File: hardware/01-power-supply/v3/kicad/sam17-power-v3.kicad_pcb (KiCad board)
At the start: 2 copper layers, 200 x 150 mm, 114 parts, among them J1 Barrier block 3 pos, J2 Molex KK-254 4 pos, J3 Barrier block 3 pos, J4 Barrier block 2 pos, J5 Faston macho 6.3mm PCB, J6 Molex KK-254 2 pos, J7 Barrier block 2 pos, J8 JST-PH 4 pos, U1 LM2941CT/NOPB, U10 ADS1115IDGSR — ADC 16 bits 4 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, U11 TMP1075DGKR — sensor de tempe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, U12 ISO1541D — aislador I2C bidir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, U2 LM2991T/NOPB, U3 LM7805, U4 LT3045EDD#TRPBF, U5 LT3045EDD#TRPBF, U6 LT3094EDD#PBF, U7 LT3094EDD#PBF, U8 INA226AIDGSR — monitor I/V I2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, U9 INA226AIDGSR — monitor I/V I2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

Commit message: Cero conexiones sin rutear, y el filler de KiCad se cae con la placa terminada
126 elementos sin conectar -> 0. DRC real: 48 infracciones -> 10, y ninguna
de las diez es de cobre.

    clearance          0     (eran 34)
    cortos             0
    hole_to_hole       0     (era 1)
    sin conectar       0     (eran 126)
    silk_overlap       5     cosmetica, pendiente
    track_dangling     3     tres rabitos de 0.5 mm sin enganchar
    isolated_copper    1     la zona GNDREF, ver abajo

## Tres cosas que estaban mal y no eran del ruteo

**El EP de U6/U7 no llegaba a ningun sitio.** Salia 2.5 mm al sur y ahi se
quedaba: la entrada de los dos LT3094 estaba conectada solo por sus pines
1-3. Las puertas propias no lo veian porque miden SEPARACION, no
continuidad; el DRC real si. Ahora baja a y=55.5 -- por debajo de la fila de
pines, que acaba en 54.25 -- y entra al canal vertical de su mitad de la isla.

**F1 tiene dos clips por lado.** Su huella trae dos pads numerados "1" y dos
numerados "2", y la cadena de red entraba por uno de cada par: el
portafusible tiene dos posiciones y solo una estaba cableada.

**+12V eran dos islas.** El canal de x=19.5 con R15.2 y D10.2 por un lado, y
el de x=41.5 con R16.2, el shunt y TP3 por otro, sin nada que los una. El
laberinto no lo veia porque cada pad tocaba ALGUN cobre de su red: ahora se
calculan los componentes conexos y solo el mayor cuenta como "ya conectado".

## Dos trampas de la herramienta, las dos medidas

**`ZONE_FILLER.Fill()` hace SEGFAULT** desde el Python de KiCad 10.0 con esta
placa ya ruteada: exit 139, sin traceback, con 1042 segmentos (con 995
todavia pasaba). No es la zona -- quitando el recorte de H4 tambien peta, y
sin la zona la placa sale entera en verde. El relleno se delega a
`kicad-cli pcb drc --refill-zones --save-board`, que es el mismo codigo
fuera del proceso y no se cae.

**Y la netclass se escapo por segunda vez.** La ronda anterior la escribia en
el .kicad_pro; `kicad-cli --save-board` la devolv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
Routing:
- net /GNDREF: track 0.00 -> 116.0 mm, vias 0 -> 8
- net +12V: track 226.6 -> 260.8 mm, vias 4 -> 6
- net /-12V9: track 383.3 -> 393.3 mm
- net Net-(U7-ILIM): track 5.71 -> 12.2 mm, vias 0 -> 2
- net /L_F: track 123.4 -> 128.5 mm
- net /L: track 32.0 -> 37.1 mm
- net Net-(U6-ILIM): vias 0 -> 2

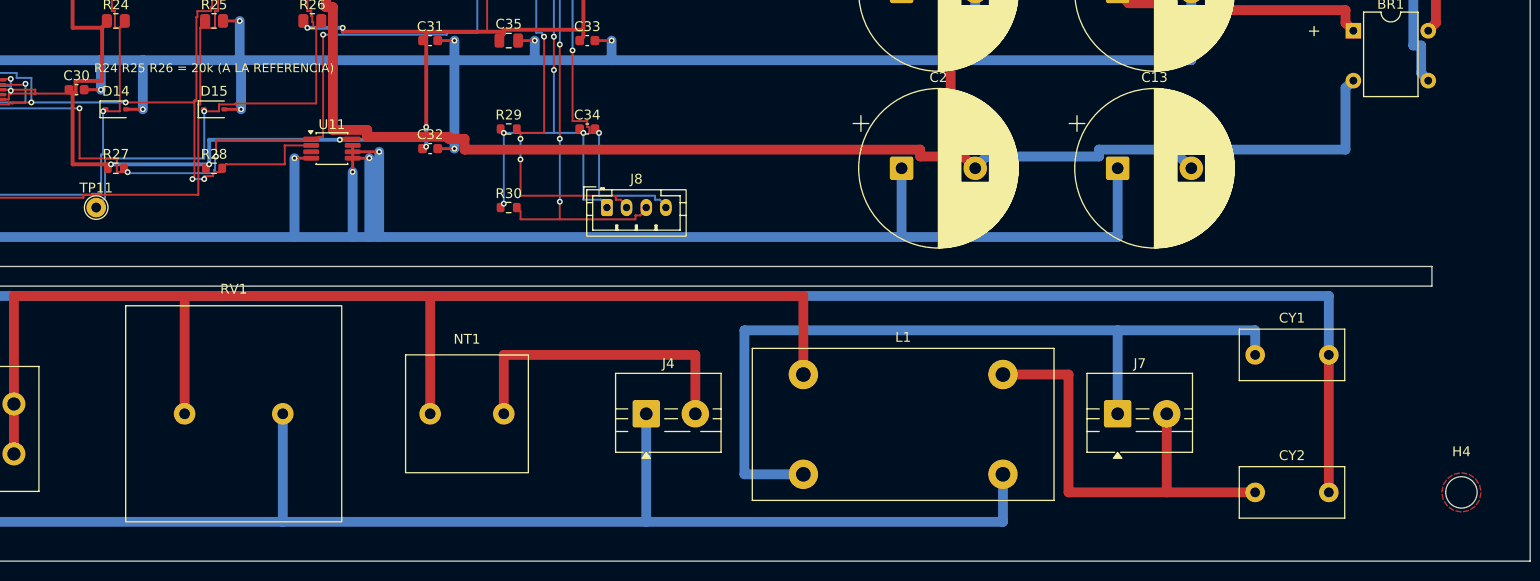
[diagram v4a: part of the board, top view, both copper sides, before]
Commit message: La isla de referencia se rellenaba a 140 mm de donde tenia que estar
DRC real: 0 infracciones y 0 elementos sin conectar. Eran 48 y 126 al
empezar la fase.

## El recorte de H4 apuntaba fuera de su propio poligono

La zona de GNDREF cubre ISLA_REF, que son 3256 mm2 sobre (10,12)-(54,86). Lo
que habia en la placa era **un trozo de 12.24 mm2 centrado en (193, 143)**,
o sea alrededor del taladro H4 y en la esquina opuesta.

El recorte circular de H4 se escribio cuando la placa media 150x200 y el
taladro caia dentro de la isla. Al girarla a 200x150 (Task 6) H4 se fue a
(193, 143) y el recorte se quedo: un "agujero" fuera del contorno que lo
contiene, que es geometria invalida. El comentario del codigo seguia diciendo
"H4 cae DENTRO de ISLA_REF" -- ya no.

De ahi salian, todos a la vez, el `isolated_copper` del DRC y los seis pads
de GNDREF sin conectar. Ahora el recorte se calcula: se recorta el taladro
que de verdad caiga dentro, y si no cae ninguno no se recorta ninguno. Son
cero. La zona pasa a rellenar 1664.8 mm2 en dos trozos, el mayor de 1514 mm2
centrado en (28.5, 43.4).

**El segfault del ZONE_FILLER no era esto.** Se probo a proposito con el
poligono ya arreglado y se sigue cayendo: son dos fallos independientes y el
relleno se queda delegado en `kicad-cli --refill-zones --save-board`.

## Lo demas de esta ronda

* **Tres rabitos de 0.5 mm colgando.** El remate al centro del pad se
  insertaba en el primer tramo del camino, y ese tramo puede estar en B.Cu:
  una pista de B.Cu naciendo en un pad SMD que solo existe en F.Cu. Ahora se
  remata solo en una capa donde el pad tenga cobre. (Y el primer intento
  comparaba un entero de capa contra un nombre: siempre falso, dejo de
  rematar en los 19 sitios donde si hacia falta. Corregido.)
* **Seis choques de serigrafia.** Las referencias de C2 y C13 caian entre la
  seda del bulk de arriba y la del suyo -- 0.45 mm sobre un minimo de 0.5 --
  y debajo tampoco cabian: ahi empieza la ranura de la barrera de red. Van al
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
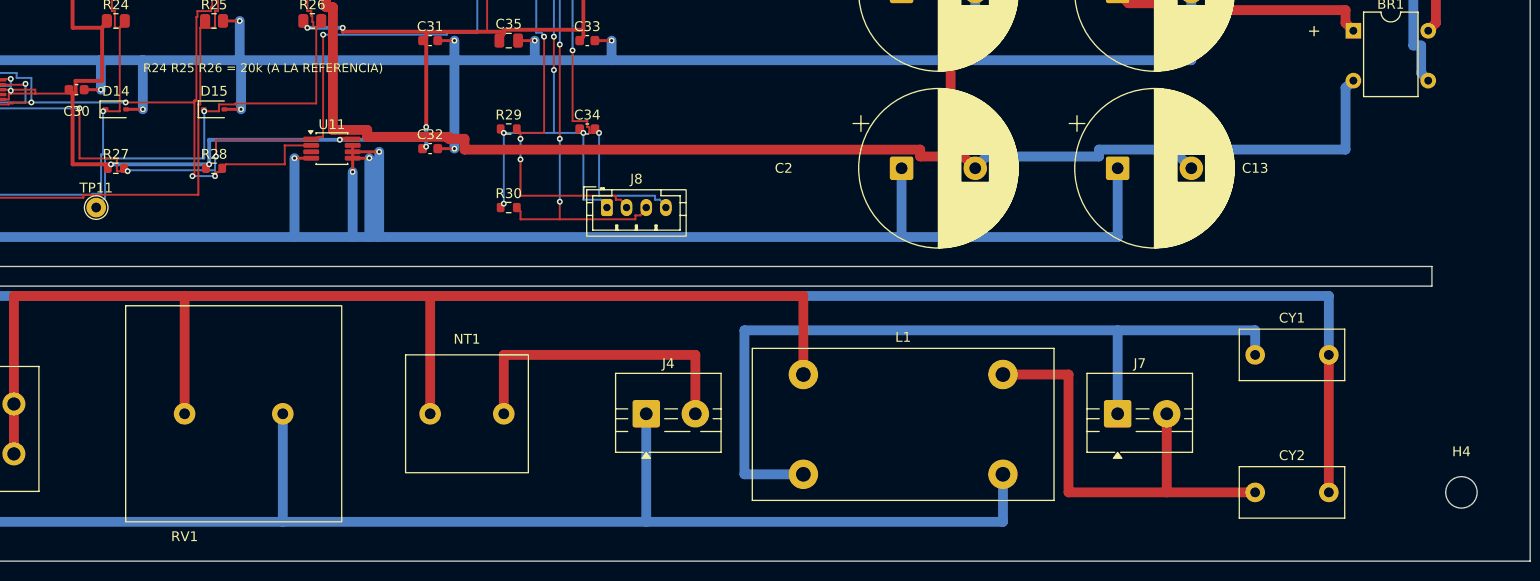
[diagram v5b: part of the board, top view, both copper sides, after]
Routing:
- net +3V3: track 48.6 -> 47.5 mm
- net /SCL_A: track 141.7 -> 141.1 mm
- net /SDA_A: track 132.3 -> 131.7 mm
- net +5V: track 345.4 -> 344.9 mm

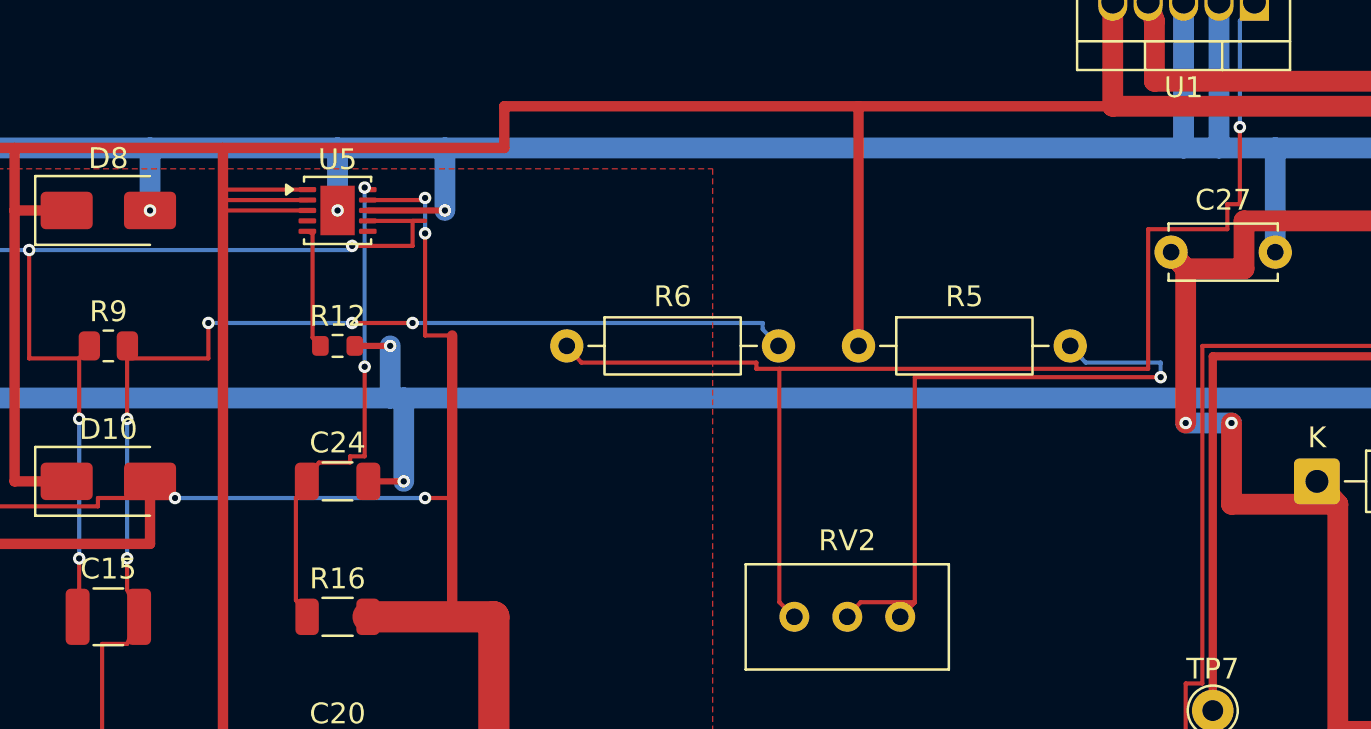
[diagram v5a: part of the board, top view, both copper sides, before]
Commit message: R6 estaba dibujado espejado de R8, y su pad de referencia nunca estuvo conectado
DRC real: 0 infracciones, 0 elementos sin conectar. Todas las puertas propias
en verde, incluida `revisar_isla_referencia()`, que era la ultima en rojo.

## El hallazgo

R6 y R8 son el mismo divisor de ajuste a cada lado de la placa, con la misma
huella y la misma colocacion. En el esquematico estan dibujados espejados --
R6 lleva GNDREF abajo y R8 arriba -- asi que el pin que toca la referencia es
el 2 en uno y el 1 en el otro.

En la PLACA eso manda el pad de GNDREF de R6 a x=57.16. ISLA_REF acaba en
x=54: ni la zona lo alcanzaba ni una pista puede llegar sin sacar la
referencia de su isla. **R6.2 no ha estado conectado en ninguna version de
esta fuente**, y R6 es el fondo del divisor de ajuste de U1, el pre-regulador
de +12 V.

No se vio antes porque la puerta que lo vigila solo mira PISTAS de GNDREF, y
hasta esta tanda no habia ninguna: era verde por vacia. Es el Principio VIII
de la constitucion aplicandose solo -- una comprobacion que nunca se ha visto
fallar no es una comprobacion.

## El arreglo

Girar el simbolo de R6 180 grados. El cableado del esquematico no se mueve ni
un milimetro y la huella tampoco -- un resistor es simetrico -- pero el pad
que lleva GNDREF pasa a ser el 1, que esta en x=47 y dentro de la isla, igual
que el de R8.

El golden lo caza y por eso existe:

    -GNDREF:        C15-2 C16-2 JP1-1 R10-2 R6-2 R8-1 R9-2
    +GNDREF:        C15-2 C16-2 JP1-1 R10-2 R6-1 R8-1 R9-2
    -Net-(U1-ADJ):  R6-1 RV2-3 U1-1
    +Net-(U1-ADJ):  R6-2 RV2-3 U1-1

Dos lineas, y ninguna otra red se movio.

## Estado de las puertas

    check_netlist.py   OK -- shunts en serie, tres divisores en su sentido,
                       los cinco chips en el I2C, barrera de masas sin un
                       nodo comun
    check_bom.py       OK -- 110 en la hoja, 114 designadores
    netdiff            golden actualizado, solo estas dos redes
    DRC (kicad-cli)    0 infracciones, 0 sin c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
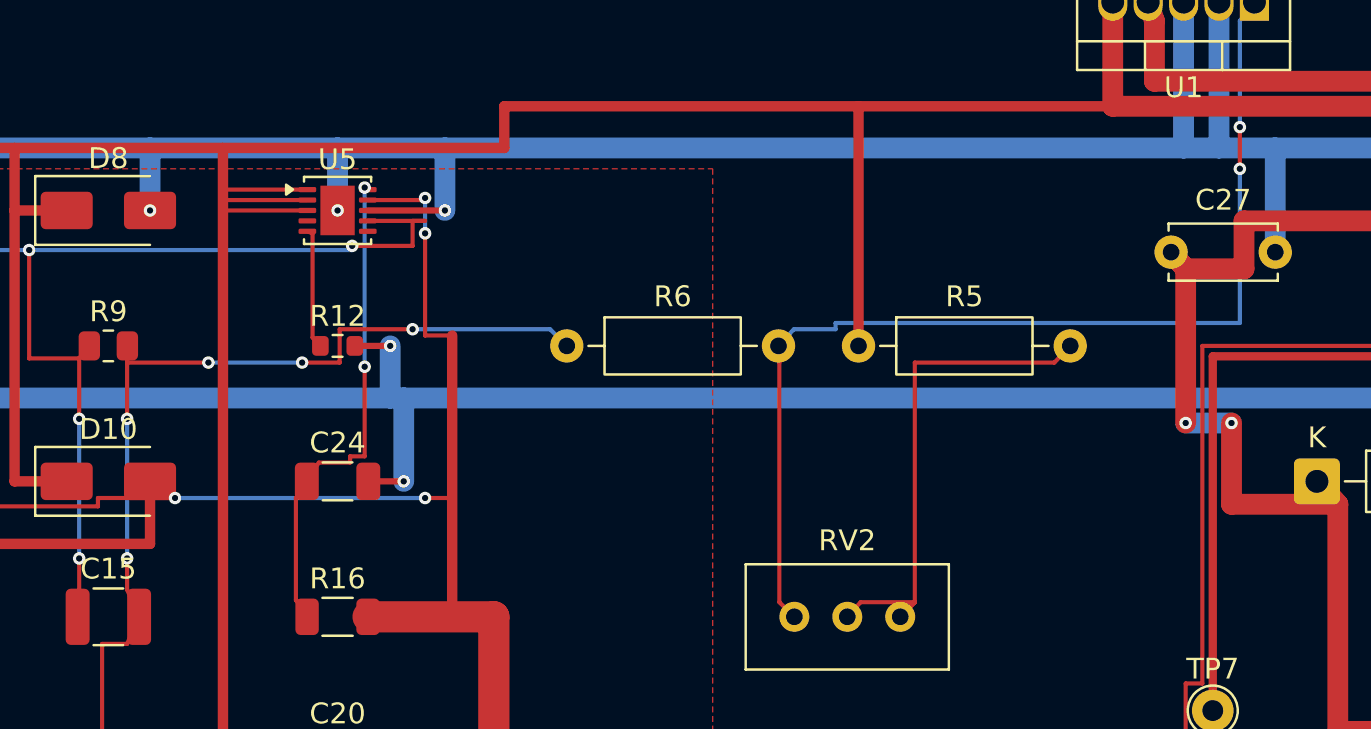
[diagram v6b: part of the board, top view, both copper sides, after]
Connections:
- R6 pad 1: Net-(U1-ADJ) -> /GNDREF
- R6 pad 2: /GNDREF -> Net-(U1-ADJ)
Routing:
- net Net-(U1-ADJ): track 63.0 -> 51.7 mm, vias 1 -> 2
- net /GNDREF: track 116.0 -> 104.8 mm
- net Net-(R5-Pad2): track 33.5 -> 24.8 mm, vias 1 -> 0

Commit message: Dos fusibles en serie en el mismo primario, y ninguno sabia cual miraba
Cierra la parte del #130 que tocaba la PCB. `F1` sale de la placa: el fusible
de red se queda en el IEC C14 de la pared del recinto.

## El desfase

La spec del case §7 lo dice desde el principio, dos veces -- "entrada IEC C14
con portafusible + interruptor" -- y `F1` estaba ademas en la placa. Nadie
habia cruzado los dos documentos. Dos fusibles en serie en el mismo primario
es peor que uno solo: el mismo fallo los ve a los dos y no hay forma de saber
cual miro.

Se queda el del IEC porque es el ACCESIBLE. Cambiar `F1` obligaba a abrir un
recinto de acero cerrado.

**El requisito no se va con la pieza**, y eso queda escrito en design-notes
§14.2 y en el README de fab: el fusible del chasis tiene que ser 1.6 A lento
-- por el inrush del toroide de 120 VA mas los 0.2 A de la SMPS -- y su
portafusible **cerrado**, que es lo que pide haber elegido aislamiento
reforzado. Si el IEC que se compre no cumple las dos, no vale: la placa ya no
tiene red detras.

## Lo que cambia

    redes            60 -> 59   (`L` y `L_F` eran el mismo nodo sin F1 en medio)
    nodos           303 -> 301
    pads de red      23 -> 19   (los cuatro clips del portafusible)
    DRC               0 infracciones, 0 sin conectar
    las 7 puertas     en verde

`L_F` significaba "L despues del fusible" y aqui ya no hay fusible: lo que
entra por J3 es `L`, sin mas. El invariante de `check_netlist.py` se reescribe
contra ese nombre y sigue vigilando LO MISMO -- de que nodo cuelga el choke de
la SMPS: antes de NT1, porque el limitador esta dimensionado para TR1 y la
SMPS no debe compartirlo (spec v2 §7).

## Y una regla que medía la serigrafía

Al re-rutear salio que `revisar_diagonal()` habia bajado de 40 a 32 mm sobre
un umbral de 30. La causa no era electrica: `bbox_de()` usaba
`GetBoundingBox()` a secas, que **cuenta el texto**, y en la ronda anterior yo
habia movido la referencia "C2" por un choque de serigrafia. Ocho milimet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
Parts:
- removed F1: Fusible 1.6A lento + portafusible CERRADO 5x20, Fuseholder_Cylinder-5x20mm_Schurter_FPG4_Vertical_Closed
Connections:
- L1 pad 1: /L_F -> /L
- NT1 pad 1: /L_F -> /L
- RV1 pad 1: /L_F -> /L
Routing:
- net /L_F: track 128.5 -> 0.00 mm
- net /L: track 37.1 -> 150.0 mm

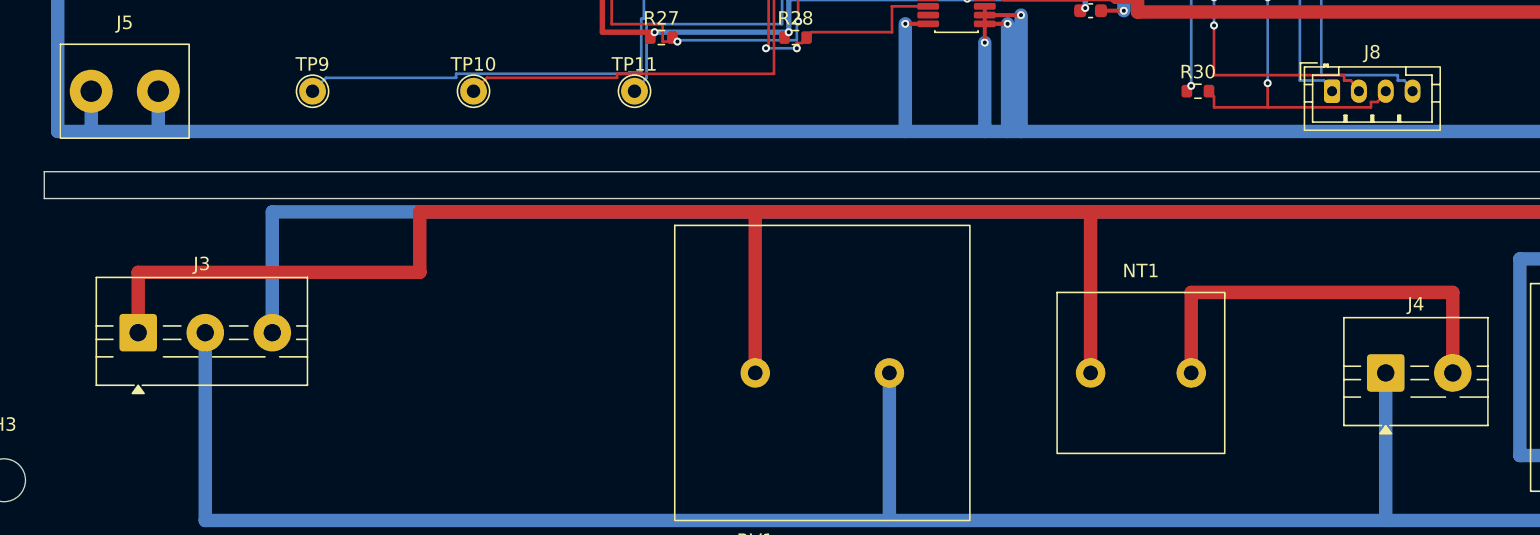
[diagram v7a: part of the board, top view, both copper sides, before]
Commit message: La placa regenerada con las huellas buenas, y un literal que dependia de una
NT1 movio un pad 2,4 mm al pasar a su huella real (paso 5,1 y no 7,5), asi que
esto es esquematico, netlist, placa, relleno de zona y las siete salidas de
fabricacion otra vez.

Y saco a la luz una cota escrita dos veces: el 95.5 de rutear_red() era la x
del pad 2 CON LA HUELLA VIEJA. Al mover el paso, la subida de NT1.2 arrancaba
en el aire. Ahora se pide con pad_xy(), como sus dos vecinos de arriba -- un
literal que depende de una huella es la misma cota en dos sitios, y solo uno
de los dos se entera cuando cambia.

  DRC (kicad-cli, --severity-all)   0 infracciones  0 sin conectar  0 paridad
  ruteo                             1024 segmentos (antes 1033), 176 vias
  netdiff                           VERDE -- la conectividad no se movio
  barrera de red                    10,63 mm entre pads
                                     7,99 mm sobre el cobre del gerber
  zona GNDREF en el gerber          2159 mm2 de cobre relleno
  cpl                               42 designadores, ninguno con rotacion != 0

El .drl cambia en tres sitios y por eso habia que reexportarlo: el MOV pasa de
1,1 a 1,3, el faston de 1,6 a 1,3 y el NTC de 1,1 a 0,8. Un taladro solo
existe en el drill: el .kicad_pcb no se manda a fabricar.

Co-Authored-By: Claude Sonnet 5 <noreply@anthropic.com>
Claude-Session: https://claude.ai/code/session_01B8kQ36zt3gJuqVVwrKaJzk
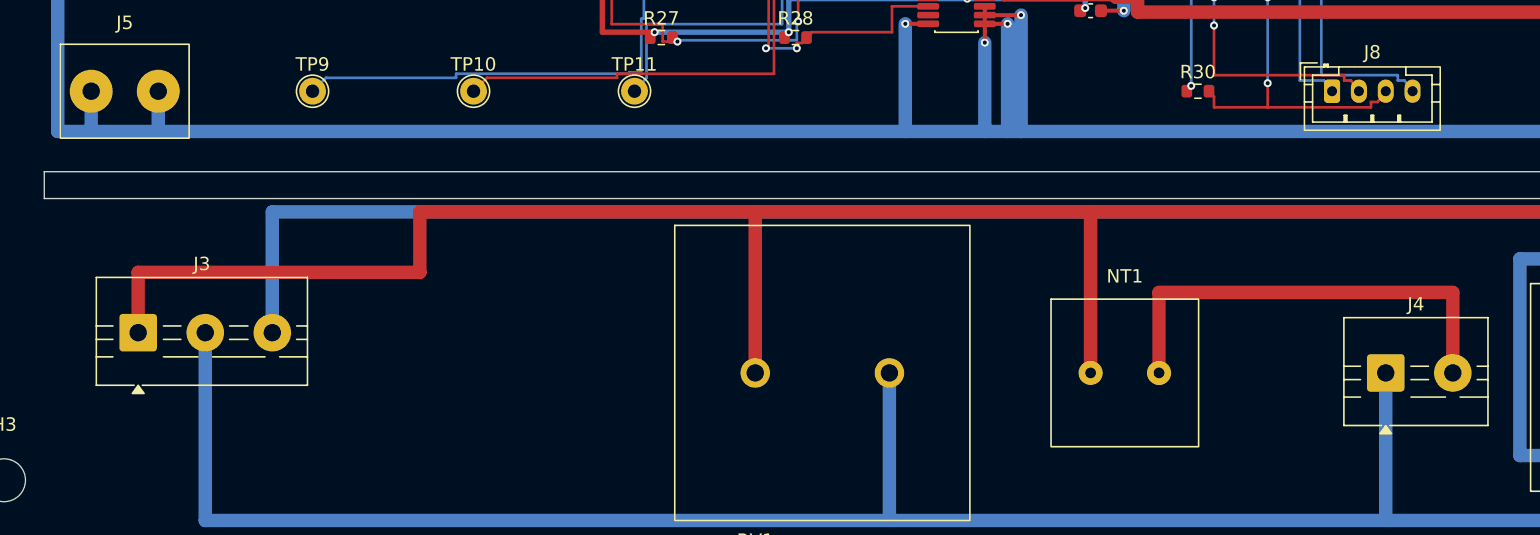
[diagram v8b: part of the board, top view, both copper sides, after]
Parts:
- J5: value Faston macho 6.3mm PCB -> Vogt 3866A.68 faston 6.3x0.8 PCB
- NT1: value SL10-5R020 -> Ametherm SL10 5R002; footprint NTC_Disc_D11.5mm_W4.5mm_P7.5mm -> NTC_Disc_D10.0mm_W4.0mm_P5.1mm
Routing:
- net /L_TR: track 31.5 -> 33.9 mm
